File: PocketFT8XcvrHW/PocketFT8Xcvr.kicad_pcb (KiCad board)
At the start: 4 copper layers, 100 x 69.9 mm, 60 parts, among them J1 HX8357D SPI, J2 22-23-2021, J3 B5B-XH-A_LF__SN_, J5 HX8357D 8-BIT, Q1 2N3904, Q2 2N3906, Q3 2N7000, Q4 2N7000, U1 MCP3422A1T-E/SN, U2 Si4735-D60-GU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

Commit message: DRC Cleanup
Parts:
- added C18: 0.1UF, Capacitor_SMD:C_0603_1608Metric, F.Cu at (124.8, 66.2)
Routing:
- net GND: track 73.0 -> 74.6 mm
- net +5V: track 226.6 -> 228.2 mm, vias 7 -> 8

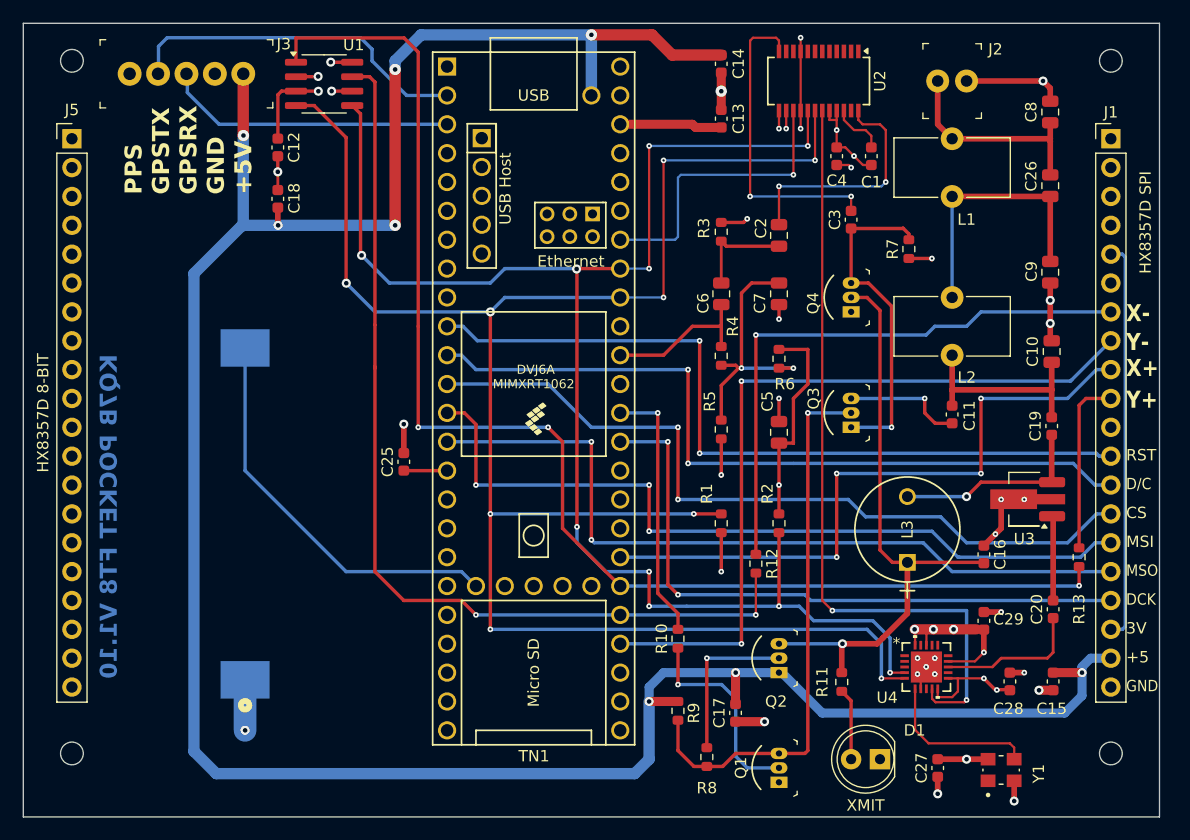
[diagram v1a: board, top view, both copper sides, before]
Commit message: 3mm mounting holes to match display
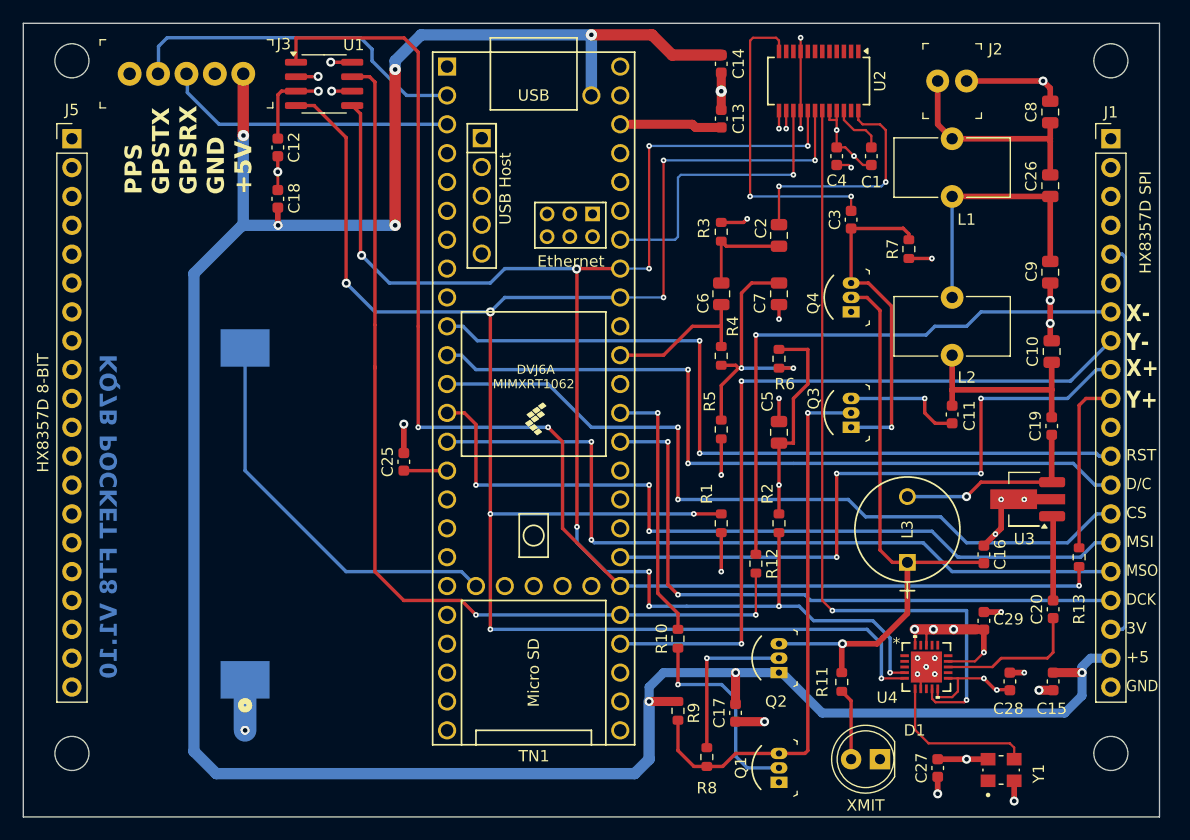
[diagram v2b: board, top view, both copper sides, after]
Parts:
- REF** (x4): value MountingHole_2mm -> MountingHole_3mm; footprint MountingHole:MountingHole_2mm -> MountingHole:MountingHole_3mm
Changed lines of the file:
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@@
 		)
 	)
-	(footprint "MountingHole:MountingHole_2mm"
+	(footprint "MountingHole:MountingHole_3mm"
 		(layer "F.Cu")
 		(at 106.68 115.062)
-		(descr "Mounting Hole 2mm, no annular")
-		(tags "mounting hole 2mm no annular")
+		(descr "Mounting Hole 3mm, no annular")
+		(tags "mounting hole 3mm no annular")
 		(property "Reference" "REF**"
-			(at 0 -3.2 0)
+			(at 0 -4 0)
 			(layer "F.SilkS")
 			(hide yes)
@@
 			)
 		)
-		(property "Value" "MountingHole_2mm"
-			(at 0 3.1 0)
+		(property "Value" "MountingHole_3mm"
+			(at 0 4 0)
 			(layer "F.Fab")
-			(hide yes)
 			(effects
 				(font
@@
 			)
 		)
-		(property "Footprint" "MountingHole:MountingHole_2mm"
+		(property "Footprint" "MountingHole:MountingHole_3mm"
 			(at 0 0 0)
 			(unlocked yes)
@@
 			)
 		)
-		(attr board_only exclude_from_pos_files exclude_from_bom)
+		(attr exclude_from_pos_files exclude_from_bom)
 		(fp_circle
 			(center 0 0)
-			(end 2 0)
+			(end 3 0)
 			(stroke
 				(width 0.15)
@@
 		(fp_circle
 			(center 0 0)
-			(end 2.25 0)
+			(end 3.25 0)
 			(stroke
 				(width 0.05)
@@
 		(pad "" np_thru_hole circle
 			(at 0 0)
-			(size 2 2)
-			(drill 2)
-			(layers "*.Mask" "F.Cu" "In1.Cu" "In2.Cu" "B.Cu")
+			(size 3 3)
+			(drill 3)
+			(layers "*.Cu" "*.Mask")
 		)
 	)
@@
 		)
 	)
-	(footprint "MountingHole:MountingHole_2mm"
+	(footprint "MountingHole:MountingHole_3mm"
 		(layer "F.Cu")
 		(at 106.68 54.102)
-		(descr "Mounting Hole 2mm, no annular")
-		(tags "mounting hole 2mm no annular")
+		(descr "Mounting Hole 3mm, no annular")
+		(tags "mounting hole 3mm no annular")
 		(property "Reference" "REF**"
-			(at 0 -3.2 0)
+			(at 0 -4 0)
 			(layer "F.SilkS")
 			(hide yes)
@@
 			)
 		)
-		(property "Value" "MountingHole_2mm"
-			(at 0 3.1 0)
+		(property "Value" "MountingHole_3mm"
+			(at 0 4 0)
 			(layer "F.Fab")
-			(hide yes)
 			(effects
 				(font
@@
 			)
 		)
-		(property "Footprint" "MountingHole:MountingHole_2mm"
+		(property "Footprint" "MountingHole:MountingHole_3mm"
 			(at 0 0 0)
 			(unlocked yes)
@@
 			)
 		)
-		(attr board_only exclude_from_pos_files exclude_from_bom)
+		(attr exclude_from_pos_files exclude_from_bom)
 		(fp_circle
 			(center 0 0)
-			(end 2 0)
+			(end 3 0)
 			(stroke
 				(width 0.15)
@@
 		(fp_circle
 			(center 0 0)
-			(end 2.25 0)
+			(end 3.25 0)
 			(stroke
 				(width 0.05)
@@
 		(pad "" np_thru_hole circle
 			(at 0 0)
-			(size 2 2)
-			(drill 2)
-			(layers "*.Mask" "F.Cu" "In1.Cu" "In2.Cu" "B.Cu")
+			(size 3 3)
+			(drill 3)
+			(layers "*.Cu" "*.Mask")
 		)
 	)
@@
 		)
 	)
-	(footprint "MountingHole:MountingHole_2mm"
+	(footprint "MountingHole:MountingHole_3mm"
 		(layer "F.Cu")
 		(at 198.12 115.062)
-		(descr "Mounting Hole 2mm, no annular")
-		(tags "mounting hole 2mm no annular")
+		(descr "Mounting Hole 3mm, no annular")
+		(tags "mounting hole 3mm no annular")
 		(property "Reference" "REF**"
-			(at 0 -3.2 0)
+			(at 0 -4 0)
 			(layer "F.SilkS")
 			(hide yes)
@@
 			)
 		)
-		(property "Value" "MountingHole_2mm"
-			(at 0 3.1 0)
+		(property "Value" "MountingHole_3mm"
+			(at 0 4 0)
 			(layer "F.Fab")
-			(hide yes)
 			(effects
 				(font
@@
 			)
 		)
-		(property "Footprint" "MountingHole:MountingHole_2mm"
+		(property "Footprint" "MountingHole:MountingHole_3mm"
 			(at 0 0 0)
 			(unlocked yes)
@@
 			)
 		)
-		(attr board_only exclude_from_pos_files exclude_from_bom)
+		(attr exclude_from_pos_files exclude_from_bom)
 		(fp_circle
 			(center 0 0)
-			(end 2 0)
+			(end 3 0)
 			(stroke
 				(width 0.15)
@@
 		(fp_circle
 			(center 0 0)
-			(end 2.25 0)
+			(end 3.25 0)
 			(stroke
 				(width 0.05)
@@
 		(pad "" np_thru_hole circle
 			(at 0 0)
-			(size 2 2)
-			(drill 2)
-			(layers "*.Mask" "F.Cu" "In1.Cu" "In2.Cu" "B.Cu")
+			(size 3 3)
+			(drill 3)
+			(layers "*.Cu" "*.Mask")
 		)
 	)
@@
 		)
 	)
-	(footprint "MountingHole:MountingHole_2mm"
+	(footprint "MountingHole:MountingHole_3mm"
 		(layer "F.Cu")
 		(at 198.12 54.102)
-		(descr "Mounting Hole 2mm, no annular")
-		(tags "mounting hole 2mm no annular")
+		(descr "Mounting Hole 3mm, no annular")
+		(tags "mounting hole 3mm no annular")
 		(property "Reference" "REF**"
-			(at 0 -3.2 0)
+			(at 0 -4 0)
 			(layer "F.SilkS")
 			(hide yes)
@@
 			)
 		)
-		(property "Value" "MountingHole_2mm"
-			(at 0 3.1 0)
+		(property "Value" "MountingHole_3mm"
+			(at 0 4 0)
 			(layer "F.Fab")
-			(hide yes)
 			(effects
 				(font
@@
 			)
 		)
-		(property "Footprint" "MountingHole:MountingHole_2mm"
+		(property "Footprint" "MountingHole:MountingHole_3mm"
 			(at 0 0 0)
 			(unlocked yes)
@@
 			)
 		)
-		(attr board_only exclude_from_pos_files exclude_from_bom)
+		(attr exclude_from_pos_files exclude_from_bom)
 		(fp_circle
 			(center 0 0)
-			(end 2 0)
+			(end 3 0)
 			(stroke
 				(width 0.15)
@@
 		(fp_circle
 			(center 0 0)
-			(end 2.25 0)
+			(end 3.25 0)
 			(stroke
 				(width 0.05)
@@
 		(pad "" np_thru_hole circle
 			(at 0 0)
-			(size 2 2)
-			(drill 2)
+			(size 3 3)
+			(drill 3)
 			(layers "*.Cu" "*.Mask")
 		)

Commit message: Pivot to 74ACT244DWR Power Amplifier (in progress)
ToDo:  LPF values, bifilar transformer specs, QA checks (esp. XMIT/RECV logic)
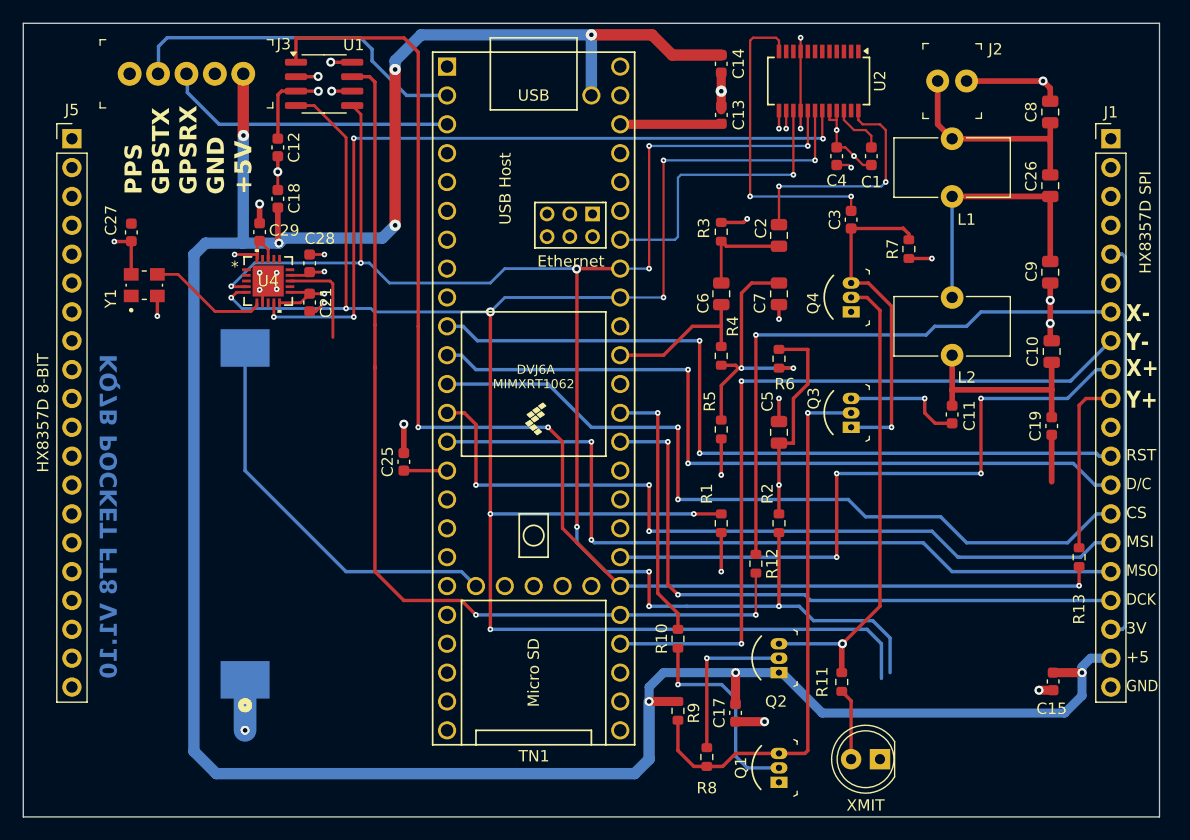
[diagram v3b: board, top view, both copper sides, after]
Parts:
- removed C16, C20: 0.1UF, Capacitor_SMD:C_0603_1608Metric
- removed L3: 1.0mH, footprints:IND_BOURNS_RLB9012
- removed REF** (x4): MountingHole_3mm, MountingHole:MountingHole_3mm
- removed U3: GVA-84+, Package_TO_SOT_SMD:SOT-89-3_Handsoldering
- added C21: 0.1UF, Capacitor_SMD:C_0603_1608Metric, F.Cu at (127.6, 75.4)
- moved Y1 86.6 mm to (113.0, 73.8)
- moved C27 85.2 mm to (111.9, 69.2), turned to -90 degrees
- moved C29 72.3 mm to (123.2, 69.2)
- moved C28 71.8 mm to (127.6, 71.9)
- moved U4 67.2 mm to (124.0, 73.5)
- moved C13 0.33 mm to (163.8, 58.9)
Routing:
- net Net-(C19-Pad1): track 17.5 -> 4.23 mm, vias 1 -> 0
- net /SCL: track 136.0 -> 148.8 mm
- net /SDA: track 166.0 -> 177.3 mm
- net /XMIT: track 53.2 -> 41.9 mm
- net +3.3V: track 79.6 -> 69.8 mm, vias 12 -> 9
- net Net-(C20-Pad2): track 7.45 -> 0.00 mm
- net GND: track 74.6 -> 68.5 mm, vias 34 -> 30
- net /XCLK: track 12.8 -> 8.60 mm
- net +5V: track 228.2 -> 232.3 mm
- net Net-(U4-CLKIN): track 14.0 -> 10.6 mm
- net /RCLK: track 68.2 -> 67.8 mm, vias 2 -> 4

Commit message: New 74ACT244 PA in progress
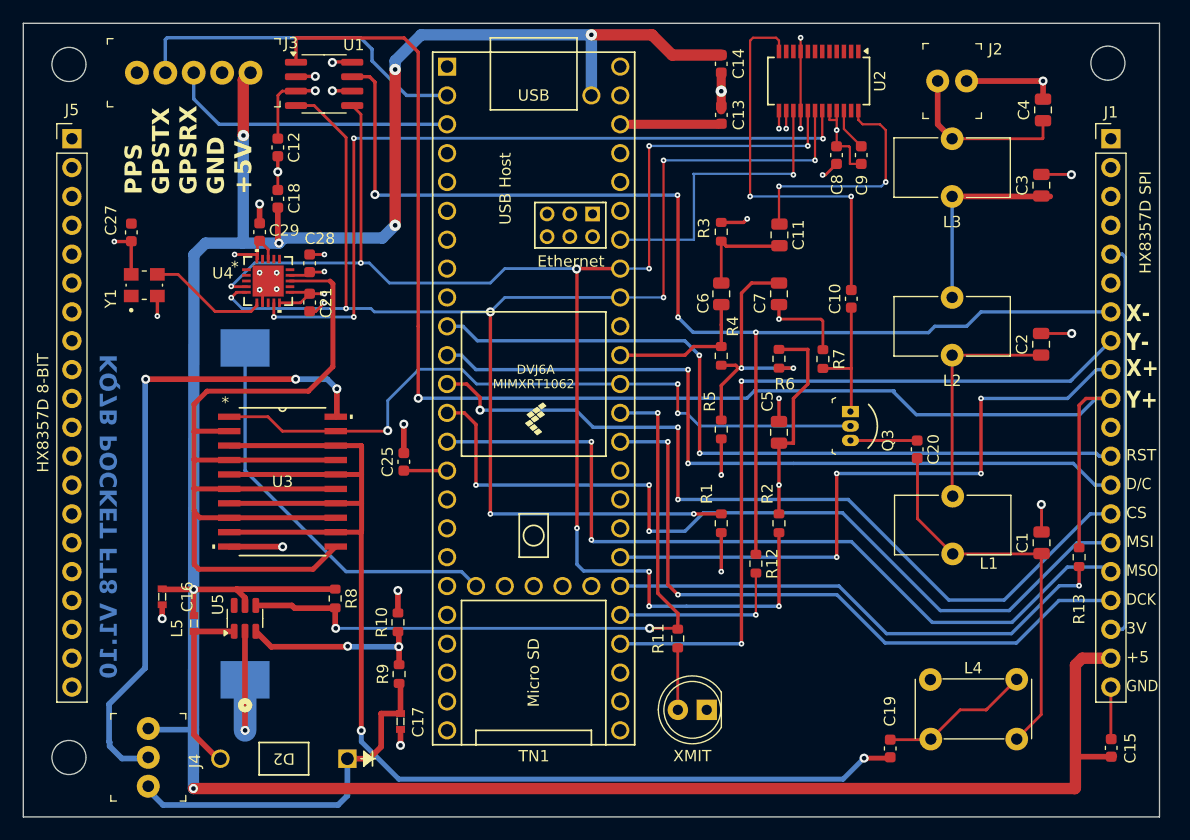
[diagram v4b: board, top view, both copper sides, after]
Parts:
- removed C26: 47PF, Capacitor_SMD:C_0805_2012Metric
- removed Q1: 2N3904, digikey-footprints:TO-92-3
- removed Q2: 2N3906, digikey-footprints:TO-92-3
- removed Q4: 2N7000, digikey-footprints:TO-92-3
- added C16: 22uF, digikey-footprints:0603, F.Cu at (114.6, 101.3)
- added C20: 0.1UF, Capacitor_SMD:C_0603_1608Metric, F.Cu at (181.1, 88.3)
- added D2: 1N5817, 1N5817T:DO-41_DIO, F.Cu at (130.9, 115.5)
- added J4: XMT PWR, digikey-footprints:PinHeader_1x3_P2.54mm_Drill1.02mm, F.Cu at (113.4, 118.0)
- added L3: 1.2uh, Inductor_THT:L_Toroid_Vertical_L10.0mm_W5.0mm_P5.08mm, F.Cu at (184.1, 66.0)
- added L4: L_Ferrite_Coupled, Inductor_THT:L_Toroid_Vertical_BIFILAR, F.Cu at (186.0, 108.6)
- added L5: 22nH, 1.3A, digikey-footprints:0603, F.Cu at (117.4, 103.6)
- added REF**: MountingHole_3mm, MountingHole:MountingHole_3mm, F.Cu at (106.4, 54.4)
- added REF**: MountingHole_3mm, MountingHole:MountingHole_3mm, F.Cu at (106.4, 115.4)
- added REF**: MountingHole_3mm, MountingHole:MountingHole_3mm, F.Cu at (197.9, 54.3)
- added U3: SN74ACT244DWR, sn74act244dwr:DW20, F.Cu at (125.2, 91.1)
- added U5: MT3608, Package_TO_SOT_SMD:SOT-23-6, F.Cu at (121.9, 103.2)
- C1, C4: value 0.1UF -> 910pf; footprint Capacitor_SMD:C_0603_1608Metric -> Capacitor_SMD:C_0805_2012Metric
- C10, C8: value 910pf -> 0.1UF; footprint Capacitor_SMD:C_0805_2012Metric -> Capacitor_SMD:C_0603_1608Metric
- C11: value 0.1UF -> 10UF; footprint Capacitor_SMD:C_0603_1608Metric -> Capacitor_SMD:C_0805_2012Metric
- C17: value 0.1UF -> 22uF; footprint Capacitor_SMD:C_0603_1608Metric -> digikey-footprints:0603
- C2: value 10UF -> 1300pf
- C3: value 0.1UF -> 1300pf; footprint Capacitor_SMD:C_0603_1608Metric -> Capacitor_SMD:C_0805_2012Metric
- C9: value 1300pf -> 0.1UF; footprint Capacitor_SMD:C_0805_2012Metric -> Capacitor_SMD:C_0603_1608Metric
- R10, R9: value 5.1K -> 3.9K
- R8: value 510 Ohm -> 3.9K
- moved C1 37.2 mm to (192.0, 96.5)
- moved R8 35.6 mm to (129.8, 101.4)
- moved C19 31.7 mm to (178.7, 114.6)
- moved L1 31.5 mm to (184.2, 97.5)
- moved C17 29.5 mm to (135.6, 112.2), turned to -90 degrees
- moved C2 25.0 mm to (192.0, 79.0), turned to 90 degrees
- moved R9 24.8 mm to (135.5, 108.1)
- moved R10 24.7 mm to (135.4, 103.5)
- moved C11 21.9 mm to (168.9, 69.4), turned to -90 degrees
- moved C9 19.6 mm to (176.2, 62.4), turned to 90 degrees
- moved C8 19.2 mm to (174.0, 62.4)
- moved C4 18.6 mm to (192.2, 58.4)
- moved C10 18.2 mm to (175.3, 75.0)
- moved C3 17.0 mm to (192.0, 65.0)
- moved D1 15.9 mm to (162.6, 111.2)
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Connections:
- C1 pad 1: +3.3V -> Net-(C1-Pad1)
- C1 pad 2: Net-(U2-DBYP) -> GND
- C10 pad 1: Net-(C10-Pad1) -> Net-(Q3-S)
- C10 pad 2: GND -> Net-(U2-AMI)
- C11 pad 1: Net-(Q3-D) -> Net-(U2-LOUT/[DFS])
- C11 pad 2: Net-(C10-Pad1) -> Net-(C11-Pad2)
- C17 pad 1: GND -> Net-(D2-K)
- C17 pad 2: +5V -> GND
- C19 pad 1: Net-(C19-Pad1) -> /XOUT
- C19 pad 2: Net-(C10-Pad1) -> Net-(C19-Pad2)
- C2 pad 1: Net-(U2-LOUT/[DFS]) -> Net-(C2-Pad1)
- C2 pad 2: Net-(C2-Pad2) -> GND
- C3 pad 1: Net-(Q3-S) -> Net-(C3-Pad1)
- C3 pad 2: Net-(U2-AMI) -> GND
- C4 pad 1: GND -> Net-(J2-ANT)
- C4 pad 2: +3.3V -> GND
- C6 pad 1: Net-(C2-Pad2) -> Net-(C11-Pad2)
- C8 pad 1: Net-(J2-ANT) -> GND
- C8 pad 2: GND -> +3.3V
- C9 pad 1: Net-(C26-Pad1) -> +3.3V
- C9 pad 2: GND -> Net-(U2-DBYP)
- L1 pad 1: Net-(C26-Pad1) -> Net-(C1-Pad1)
- L1 pad 2: Net-(J2-ANT) -> Net-(C2-Pad1)
- L2 pad 1: Net-(C10-Pad1) -> Net-(C2-Pad1)
- L2 pad 2: Net-(C26-Pad1) -> Net-(C3-Pad1)
- Q3 pad 2: /RECV -> /RCV
- R10 pad 1: Net-(Q1-B) -> Net-(U5-FB)
- R10 pad 2: /PTT -> GND
- R11 pad 1: /XMIT -> /XMT
- R3 pad 2: Net-(C2-Pad2) -> Net-(C11-Pad2)
- R8 pad 1: Net-(Q2-B) -> +5V
- R8 pad 2: /RECV -> /XMT
- R9 pad 1: /RECV -> Net-(D2-K)
- R9 pad 2: +5V -> Net-(U5-FB)
- TN1 pad 36: /PTT -> /XMT
- TN1 pad 37: unconnected-(TN1-15_A1_RX3_SPDIF_IN-Pad37) -> /RCV
- U1 pad 1: /Y+ -> Net-(J1-Y+)
- U1 pad 7: /X- -> Net-(J1-X-)
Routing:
- net /XOUT: track 0.00 -> 121.4 mm, vias 0 -> 2
- net Net-(J1-Y+): track 15.6 -> 122.3 mm, vias 0 -> 1
- net /XCLK: track 8.60 -> 93.2 mm
- net /Y+: track 116.6 -> 45.7 mm, vias 3 -> 1
- net /X-: track 84.2 -> 15.6 mm, vias 2 -> 1
- net /RCV: track 0.00 -> 62.8 mm, vias 0 -> 3
- net /XMT: track 0.00 -> 62.1 mm, vias 0 -> 3
- net Net-(J1-X-): track 51.4 -> 108.5 mm, vias 1 -> 4
- net /+VPA: track 0.00 -> 57.0 mm, vias 0 -> 3
- net /RECV: track 48.8 -> 0.00 mm, vias 1 -> 0
- net /SDA: track 177.3 -> 129.2 mm, vias 9 -> 8
- net /XMIT: track 41.9 -> 0.00 mm, vias 1 -> 0
- net Net-(C1-Pad1): track 0.00 -> 34.7 mm
- net Net-(D2-K): track 0.00 -> 32.7 mm
- net GND: track 68.5 -> 94.1 mm, vias 30 -> 32
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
